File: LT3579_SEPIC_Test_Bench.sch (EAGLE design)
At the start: 160 parts

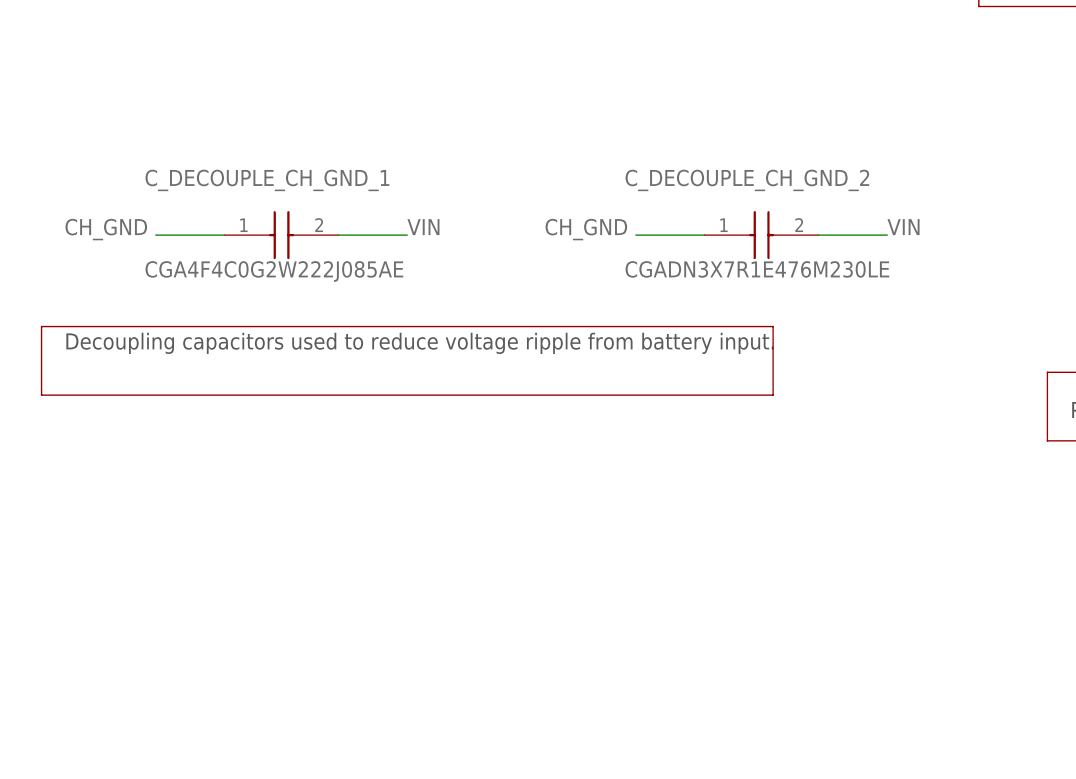
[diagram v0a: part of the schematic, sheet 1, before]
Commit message: Modified Text Sizes of Test Points, Addeed more GND Vias, Added Mounting Holes
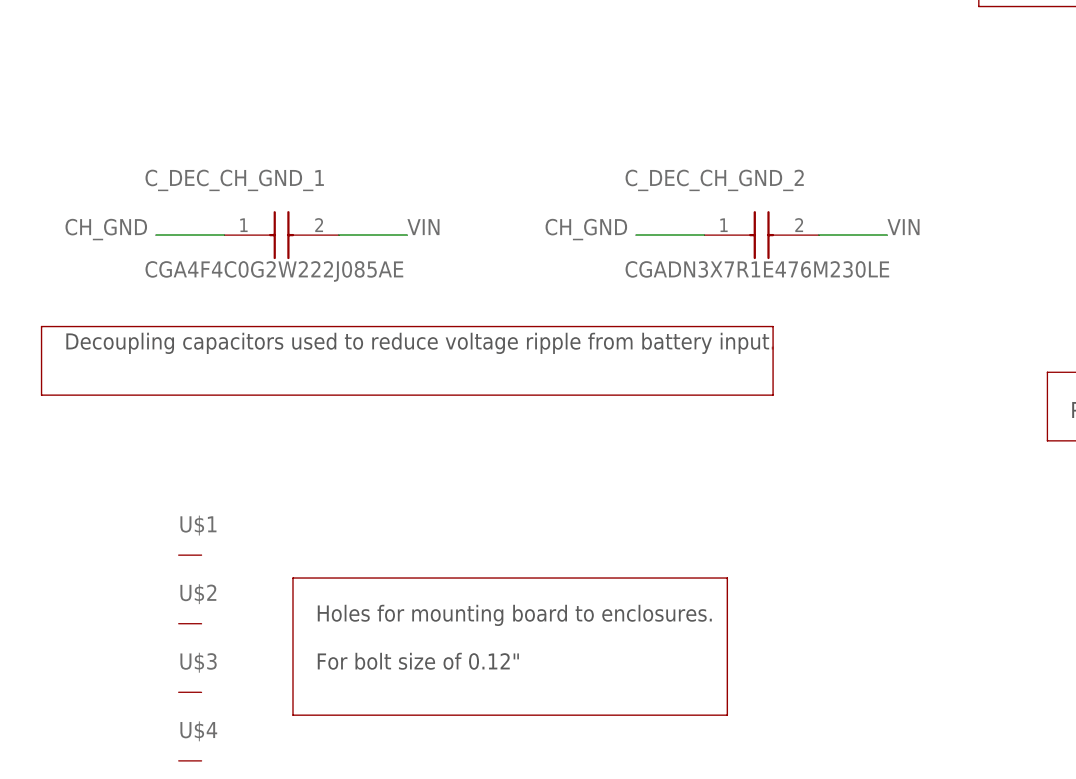
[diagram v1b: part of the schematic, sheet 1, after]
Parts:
- added U$1, U$2, U$3, U$4: THROUGH_HOLE_, THROUGH_HOLE:THROUGH_HOLE_
- renumbered C_DECOUPLE_CH_GND_1 to C_DEC_CH_GND_1, C_DECOUPLE_CH_GND_2 to C_DEC_CH_GND_2
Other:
- note added: "Holes for mounting board to enclosures. For bolt size of 0.12""
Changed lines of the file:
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@@
 <part name="R_FB_2" library="AC0805FR-0745K3L" deviceset="AC0805FR-0745K3L" device=""/>
 <part name="4P_INPUT_CONNECTOR1" library="SAMTEC-CLP-102-02-X-D" deviceset="SAMTEC-CLP-102-02-X-D" device="J"/>
-<part name="C_DECOUPLE_CH_GND_1" library="SamacSys_Parts" deviceset="CGA4F4C0G2W222J085AE" device=""/>
-<part name="C_DECOUPLE_CH_GND_2" library="SamacSys_Parts" deviceset="CGADN3X7R1E476M230LE" device=""/>
+<part name="C_DEC_CH_GND_1" library="SamacSys_Parts" deviceset="CGA4F4C0G2W222J085AE" device=""/>
+<part name="C_DEC_CH_GND_2" library="SamacSys_Parts" deviceset="CGADN3X7R1E476M230LE" device=""/>
 <part name="12P_OUTPUT_CONNECTOR1" library="SamacSys_Parts" deviceset="CLP-106-02-F-D" device=""/>
 <part name="GND2" library="supply1" library_urn="urn:adsk.eagle:library:371" deviceset="GND" device=""/>
@@
 <part name="NMOS_LDO_2" library="SamacSys_Parts" deviceset="RSR025N03HZGTL" device=""/>
 <part name="PMOS_REVERSE_V_PROTECTION" library="DMP3015LSSQ-13" deviceset="DMP3015LSSQ-13" device=""/>
+<part name="U$1" library="THROUGH_HOLE" deviceset="THROUGH_HOLE_" device=""/>
+<part name="U$2" library="THROUGH_HOLE" deviceset="THROUGH_HOLE_" device=""/>
+<part name="U$3" library="THROUGH_HOLE" deviceset="THROUGH_HOLE_" device=""/>
+<part name="U$4" library="THROUGH_HOLE" deviceset="THROUGH_HOLE_" device=""/>
 </parts>
 <sheets>
@@
 <wire x1="7.62" y1="40.64" x2="7.62" y2="48.26" width="0.1524" layer="94"/>
 <wire x1="7.62" y1="48.26" x2="-30.48" y2="48.26" width="0.1524" layer="94"/>
+<text x="-66.04" y="-66.04" size="1.778" layer="97">Holes for mounting board to enclosures.
+For bolt size of 0.12"</text>
+<wire x1="-68.58" y1="-55.88" x2="-68.58" y2="-71.12" width="0.1524" layer="94"/>
+<wire x1="-68.58" y1="-71.12" x2="-20.32" y2="-71.12" width="0.1524" layer="94"/>
+<wire x1="-20.32" y1="-71.12" x2="-20.32" y2="-55.88" width="0.1524" layer="94"/>
+<wire x1="-20.32" y1="-55.88" x2="-68.58" y2="-55.88" width="0.1524" layer="94"/>
 </plain>
 <instances>
@@
 <attribute name="VALUE" x="-68.58" y="22.86" size="2.286" layer="96"/>
 </instance>
-<instance part="C_DECOUPLE_CH_GND_1" gate="G$1" x="-76.2" y="-17.78" smashed="yes">
+<instance part="C_DEC_CH_GND_1" gate="G$1" x="-76.2" y="-17.78" smashed="yes">
 <attribute name="NAME" x="-85.09" y="-11.43" size="1.778" layer="95" align="center-left"/>
 <attribute name="VALUE" x="-85.09" y="-21.59" size="1.778" layer="96" align="center-left"/>
 </instance>
-<instance part="C_DECOUPLE_CH_GND_2" gate="G$1" x="-22.86" y="-17.78" smashed="yes">
+<instance part="C_DEC_CH_GND_2" gate="G$1" x="-22.86" y="-17.78" smashed="yes">
 <attribute name="NAME" x="-31.75" y="-11.43" size="1.778" layer="95" align="center-left"/>
 <attribute name="VALUE" x="-31.75" y="-21.59" size="1.778" layer="96" align="center-left"/>
@@
 <attribute name="VALUE" x="34.29" y="-8.89" size="1.778" layer="96"/>
 <attribute name="NAME" x="49.53" y="-24.13" size="1.778" layer="95"/>
+</instance>
+<instance part="U$1" gate="G$1" x="-81.28" y="-53.34" smashed="yes">
+<attribute name="NAME" x="-81.28" y="-50.8" size="1.778" layer="95"/>
+</instance>
+<instance part="U$2" gate="G$1" x="-81.28" y="-60.96" smashed="yes">
+<attribute name="NAME" x="-81.28" y="-58.42" size="1.778" layer="95"/>
+</instance>
+<instance part="U$3" gate="G$1" x="-81.28" y="-68.58" smashed="yes">
+<attribute name="NAME" x="-81.28" y="-66.04" size="1.778" layer="95"/>
+</instance>
+<instance part="U$4" gate="G$1" x="-81.28" y="-76.2" smashed="yes">
+<attribute name="NAME" x="-81.28" y="-73.66" size="1.778" layer="95"/>
 </instance>
 </instances>
@@
 <net name="VIN" class="4">
 <segment>
-<pinref part="C_DECOUPLE_CH_GND_1" gate="G$1" pin="2"/>
+<pinref part="C_DEC_CH_GND_1" gate="G$1" pin="2"/>
 <wire x1="-63.5" y1="-17.78" x2="-55.88" y2="-17.78" width="0.1524" layer="91"/>
 <label x="-55.88" y="-17.78" size="1.778" layer="95"/>
 </segment>
 <segment>
-<pinref part="C_DECOUPLE_CH_GND_2" gate="G$1" pin="2"/>
+<pinref part="C_DEC_CH_GND_2" gate="G$1" pin="2"/>
 <wire x1="-10.16" y1="-17.78" x2="-2.54" y2="-17.78" width="0.1524" layer="91"/>
 <label x="-2.54" y="-17.78" size="1.778" layer="95"/>
@@
 <net name="CH_GND" class="2">
 <segment>
-<pinref part="C_DECOUPLE_CH_GND_1" gate="G$1" pin="1"/>
+<pinref part="C_DEC_CH_GND_1" gate="G$1" pin="1"/>
 <wire x1="-76.2" y1="-17.78" x2="-83.82" y2="-17.78" width="0.1524" layer="91"/>
 <label x="-93.98" y="-17.78" size="1.778" layer="95"/>
 </segment>
 <segment>
-<pinref part="C_DECOUPLE_CH_GND_2" gate="G$1" pin="1"/>
+<pinref part="C_DEC_CH_GND_2" gate="G$1" pin="1"/>
 <wire x1="-22.86" y1="-17.78" x2="-30.48" y2="-17.78" width="0.1524" layer="91"/>
 <label x="-40.64" y="-17.78" size="1.778" layer="95"/>

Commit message: changed GND planes. Ready for review
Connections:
- removed net GND: 12P_OUTPUT_CONNECTOR1.10, 12P_OUTPUT_CONNECTOR1.12, 12P_OUTPUT_CONNECTOR1.8, C_68N_FILTER_.2, C_68N_FILTER_1.2, C_68N_FILTER_2.2, C_C_.2, C_C_1.2, C_C_2.2, C_F_.2, C_F_1.2, C_F_2.2, C_IN_1_.2, C_IN_1_1.2, C_IN_1_2.2, C_IN_2_.2, C_IN_2_1.2, C_IN_2_2.2, C_LDO_IN_.2, C_LDO_OUT_.2, C_LS_.2, C_LS_1.2, C_LS_2.2, C_OUT_1_.2, C_OUT_1_1.2, C_OUT_1_2.2, C_OUT_2_.2, C_OUT_2_1.2, C_OUT_2_2.2, C_OUT_3_.2, C_OUT_3_1.2, C_OUT_3_2.2, C_SS_.2, C_SS_1.2, C_SS_2.2, L1L2_.4, L1L2_1.4, L1L2_2.4, LDO_.GND, LED_.K, LED_1.K, LED_2.K, LT3579_IC_.EPAD, LT3579_IC_.SYNC, LT3579_IC_1.EPAD, LT3579_IC_1.SYNC, LT3579_IC_2.EPAD, LT3579_IC_2.SYNC, NMOS_LDO_.S, NMOS_LDO_1.S, NMOS_LDO_2.S, R_5K_FILTER_\.2, R_5K_FILTER_\1.2, R_5K_FILTER_\2.2, R_SHUNT_GND_.2, R_SHUNT_GND_1.2, R_SHUNT_GND_2.2, R_T_.2, R_T_1.2, R_T_2.2, R_UVLO2_.1, R_UVLO2_1.1, R_UVLO2_2.1, TP_GND1_.1, TP_GND1_1.1, TP_GND1_2.1, TP_GND2_.1, TP_GND2_1.1, TP_GND2_2.1, TP_GND3_.1, TP_GND3_1.1, TP_GND3_2.1, TP_GND4_.1, TP_GND4_1.1, TP_GND4_2.1, TP_GND_.1, TP_GND_1.1, TP_GND_2.1
- new net GND_: 12P_OUTPUT_CONNECTOR1.12, C_68N_FILTER_.2, C_C_.2, C_F_.2, C_IN_1_.2, C_IN_2_.2, C_LDO_IN_.2, C_LDO_OUT_.2, C_LS_.2, C_OUT_1_.2, C_OUT_2_.2, C_OUT_3_.2, C_SS_.2, L1L2_.4, LDO_.GND, LED_.K, LT3579_IC_.EPAD, LT3579_IC_.SYNC, NMOS_LDO_.S, R_5K_FILTER_\.2, R_SHUNT_GND_.2, R_T_.2, R_UVLO2_.1, TP_GND1_.1, TP_GND2_.1, TP_GND3_.1, TP_GND4_.1, TP_GND_.1
- new net GND_1: 12P_OUTPUT_CONNECTOR1.10, C_68N_FILTER_1.2, C_C_1.2, C_F_1.2, C_IN_1_1.2, C_IN_2_1.2, C_LS_1.2, C_OUT_1_1.2, C_OUT_2_1.2, C_OUT_3_1.2, C_SS_1.2, L1L2_1.4, LED_1.K, LT3579_IC_1.EPAD, LT3579_IC_1.SYNC, NMOS_LDO_1.S, R_5K_FILTER_\1.2, R_SHUNT_GND_1.2, R_T_1.2, R_UVLO2_1.1, TP_GND1_1.1, TP_GND2_1.1, TP_GND3_1.1, TP_GND4_1.1, TP_GND_1.1
- new net GND_2: 12P_OUTPUT_CONNECTOR1.8, C_68N_FILTER_2.2, C_C_2.2, C_F_2.2, C_IN_1_2.2, C_IN_2_2.2, C_LS_2.2, C_OUT_1_2.2, C_OUT_2_2.2, C_OUT_3_2.2, C_SS_2.2, L1L2_2.4, LED_2.K, LT3579_IC_2.EPAD, LT3579_IC_2.SYNC, NMOS_LDO_2.S, R_5K_FILTER_\2.2, R_SHUNT_GND_2.2, R_T_2.2, R_UVLO2_2.1, TP_GND1_2.1, TP_GND2_2.1, TP_GND3_2.1, TP_GND4_2.1, TP_GND_2.1
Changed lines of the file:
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@@
 <part name="C_DEC_CH_GND_2" library="SamacSys_Parts" deviceset="CGADN3X7R1E476M230LE" device=""/>
 <part name="12P_OUTPUT_CONNECTOR1" library="SamacSys_Parts" deviceset="CLP-106-02-F-D" device=""/>
-<part name="GND2" library="supply1" library_urn="urn:adsk.eagle:library:371" deviceset="GND" device=""/>
 <part name="R_10K_FILTER_" library="AC0805DR-0710KL" deviceset="AC0805DR-0710KL" device=""/>
 <part name="R_5K_FILTER_\" library="SamacSys_Parts" deviceset="RT1206BRD075KL" device=""/>
@@
 <attribute name="VALUE" x="29.21" y="38.1" size="1.778" layer="96" align="center-left"/>
 </instance>
-<instance part="GND2" gate="1" x="63.5" y="27.94" smashed="yes">
-<attribute name="VALUE" x="66.04" y="30.48" size="1.778" layer="96"/>
-</instance>
 <instance part="PMOS_REVERSE_V_PROTECTION" gate="G$1" x="45.72" y="-17.78" smashed="yes" rot="R90">
 <attribute name="VALUE" x="34.29" y="-8.89" size="1.778" layer="96"/>
@@
 </busses>
 <nets>
-<net name="GND" class="1">
-<segment>
-<pinref part="12P_OUTPUT_CONNECTOR1" gate="G$1" pin="8"/>
-<wire x1="50.8" y1="27.94" x2="55.88" y2="27.94" width="0.1524" layer="91"/>
-<pinref part="12P_OUTPUT_CONNECTOR1" gate="G$1" pin="10"/>
-<wire x1="50.8" y1="30.48" x2="55.88" y2="30.48" width="0.1524" layer="91"/>
-<wire x1="55.88" y1="27.94" x2="55.88" y2="30.48" width="0.1524" layer="91"/>
-<pinref part="12P_OUTPUT_CONNECTOR1" gate="G$1" pin="12"/>
-<wire x1="50.8" y1="33.02" x2="55.88" y2="33.02" width="0.1524" layer="91"/>
-<wire x1="55.88" y1="33.02" x2="55.88" y2="30.48" width="0.1524" layer="91"/>
-<wire x1="55.88" y1="30.48" x2="63.5" y2="30.48" width="0.1524" layer="91"/>
-<pinref part="GND2" gate="1" pin="GND"/>
-<junction x="55.88" y="30.48"/>
-</segment>
-</net>
 <net name="VIN" class="4">
 <segment>
@@
 <wire x1="50.8" y1="-15.24" x2="58.42" y2="-15.24" width="0.1524" layer="91"/>
 <label x="58.42" y="-15.24" size="1.778" layer="95"/>
+</segment>
+</net>
+<net name="GND_" class="0">
+<segment>
+<pinref part="12P_OUTPUT_CONNECTOR1" gate="G$1" pin="12"/>
+<wire x1="50.8" y1="33.02" x2="55.88" y2="33.02" width="0.1524" layer="91"/>
+<label x="55.88" y="33.02" size="1.778" layer="95"/>
+</segment>
+</net>
+<net name="GND_1" class="0">
+<segment>
+<pinref part="12P_OUTPUT_CONNECTOR1" gate="G$1" pin="10"/>
+<wire x1="50.8" y1="30.48" x2="55.88" y2="30.48" width="0.1524" layer="91"/>
+<label x="55.88" y="30.48" size="1.778" layer="95"/>
+</segment>
+</net>
+<net name="GND_2" class="0">
+<segment>
+<pinref part="12P_OUTPUT_CONNECTOR1" gate="G$1" pin="8"/>
+<wire x1="50.8" y1="27.94" x2="55.88" y2="27.94" width="0.1524" layer="91"/>
+<label x="55.88" y="27.94" size="1.778" layer="95"/>
 </segment>
 </net>
@@
 </segment>
 </net>
-<net name="GND" class="1">
+<net name="GND_" class="0">
 <segment>
 <pinref part="R_SHUNT_GND_" gate="G$1" pin="2"/>
@@
 <wire x1="-119.38" y1="106.68" x2="-119.38" y2="86.36" width="0.1524" layer="91"/>
 <junction x="-119.38" y="86.36"/>
+<label x="-119.38" y="91.44" size="1.778" layer="95"/>
 </segment>
 <segment>
@@
 </segment>
 </net>
-<net name="GND" class="1">
+<net name="GND_1" class="0">
 <segment>
 <pinref part="R_SHUNT_GND_1" gate="G$1" pin="2"/>
@@
 <wire x1="-111.76" y1="109.22" x2="-111.76" y2="88.9" width="0.1524" layer="91"/>
 <junction x="-111.76" y="88.9"/>
+<label x="-111.76" y="93.98" size="1.778" layer="95"/>
 </segment>
 <segment>
@@
 </segment>
 </net>
-<net name="GND" class="1">
+<net name="GND_2" class="0">
 <segment>
 <pinref part="R_SHUNT_GND_2" gate="G$1" pin="2"/>
@@
 <wire x1="-119.38" y1="101.6" x2="-119.38" y2="81.28" width="0.1524" layer="91"/>
 <junction x="-119.38" y="81.28"/>
-</segment>
-<segment>
+<label x="-116.84" y="86.36" size="1.778" layer="95"/>
+</segment>
+<segment>

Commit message: Changed Trace Widths of Signals
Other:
- note added: "Holes for mounting board to enclosures. For bolt size of 1/16""
- note removed: "Holes for mounting board to enclosures. For bolt size of 0.12""
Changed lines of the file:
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@@
 <class number="2" name="PWR_Vin_Vout" width="0.816" drill="0">
 </class>
-<class number="3" name="Signal" width="0.0463" drill="0">
+<class number="3" name="Signal" width="0.381" drill="0">
 </class>
 <class number="4" name="PWR_Vin" width="0.0463" drill="0">
@@
 <wire x1="7.62" y1="48.26" x2="-30.48" y2="48.26" width="0.1524" layer="94"/>
 <text x="-66.04" y="-66.04" size="1.778" layer="97">Holes for mounting board to enclosures.
-For bolt size of 0.12"</text>
+For bolt size of 1/16"</text>
 <wire x1="-68.58" y1="-55.88" x2="-68.58" y2="-71.12" width="0.1524" layer="94"/>
 <wire x1="-68.58" y1="-71.12" x2="-20.32" y2="-71.12" width="0.1524" layer="94"/>

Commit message: modified GND planes
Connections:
- net CH_GND: now also C_LDO_IN_.2, C_LDO_OUT_.2, LDO_.GND
- net GND_: no longer C_LDO_IN_.2, C_LDO_OUT_.2, LDO_.GND
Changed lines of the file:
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@@
-</segment>
-<segment>
-<pinref part="LDO_" gate="G$1" pin="GND"/>
-<wire x1="-190.5" y1="-58.42" x2="-195.58" y2="-58.42" width="0.1524" layer="91"/>
-<label x="-200.66" y="-58.42" size="1.778" layer="95"/>
 </segment>
 <segment>
@@
 </segment>
 <segment>
-<pinref part="C_LDO_IN_" gate="G$1" pin="2"/>
-<pinref part="X_50" gate="G$1" pin="0"/>
-<wire x1="-167.64" y1="-86.36" x2="-160.02" y2="-86.36" width="0.1524" layer="91"/>
-</segment>
-<segment>
-<pinref part="C_LDO_OUT_" gate="G$1" pin="2"/>
-<pinref part="X_49" gate="G$1" pin="0"/>
-<wire x1="-167.64" y1="-38.1" x2="-160.02" y2="-38.1" width="0.1524" layer="91"/>
-</segment>
-<segment>
 <pinref part="C_LS_" gate="G$1" pin="2"/>
 <pinref part="X_53" gate="G$1" pin="0"/>
@@
 <junction x="-121.92" y="-96.52"/>
 </segment>
+<segment>
+<pinref part="C_LDO_IN_" gate="G$1" pin="2"/>
+<pinref part="X_50" gate="G$1" pin="0"/>
+<wire x1="-167.64" y1="-86.36" x2="-160.02" y2="-86.36" width="0.1524" layer="91"/>
+<label x="-162.56" y="-81.28" size="1.778" layer="95"/>
+</segment>
+<segment>
+<pinref part="LDO_" gate="G$1" pin="GND"/>
+<wire x1="-190.5" y1="-58.42" x2="-195.58" y2="-58.42" width="0.1524" layer="91"/>
+<label x="-208.28" y="-58.42" size="1.778" layer="95"/>
+</segment>
+<segment>
+<pinref part="C_LDO_OUT_" gate="G$1" pin="2"/>
+<pinref part="X_49" gate="G$1" pin="0"/>
+<wire x1="-167.64" y1="-38.1" x2="-160.02" y2="-38.1" width="0.1524" layer="91"/>
+<label x="-162.56" y="-35.56" size="1.778" layer="95"/>
+</segment>
 </net>

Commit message: Added more GND Vias, Changes text size, moved texts, clears DRC error
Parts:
- renumbered C_68N_FILTER_ to C_68N_F_, C_68N_FILTER_1 to C_68N_F_1, C_68N_FILTER_2 to C_68N_F_2, R_10K_FILTER_ to R_10K_F_, R_10K_FILTER_1 to R_10K_F_1, R_10K_FILTER_2 to R_10K_F_2, R_5K_FILTER_\ to R_5K_F_, R_5K_FILTER_\1 to R_5K_F_1, R_5K_FILTER_\2 to R_5K_F_2, TP_CLK_FILTER_ to TP_CLK_F_, TP_CLK_FILTER_1 to TP_CLK_F_1, TP_CLK_FILTER_2 to TP_CLK_F_2

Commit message: Used SRC to change the LBR reference of each componant
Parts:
- 12P_OUTPUT_CONNECTOR1: device SamacSys_Parts:CLP-106-02-F-D -> LT3579_SEPIC_Test_Bench:CLP-106-02-F-D
- 4P_INPUT_CONNECTOR1: device SAMTEC-CLP-102-02-X-D:SAMTEC-CLP-102-02-X-DJ -> LT3579_SEPIC_Test_Bench:SAMTEC-CLP-102-02-X-DJ
- C_1_, C_1_1, C_1_2, C_IN_1_, C_IN_1_1, C_IN_1_2, C_IN_2_, C_IN_2_1, C_IN_2_2, C_OUT_1_, C_OUT_1_1, C_OUT_1_2, C_OUT_2_, C_OUT_2_1, C_OUT_2_2, C_OUT_3_, C_OUT_3_1, C_OUT_3_2: device SamacSys_Parts:CGA4J1X7R1E475K125AE -> LT3579_SEPIC_Test_Bench:CGA4J1X7R1E475K125AE
- C_68N_F_, C_68N_F_1, C_68N_F_2: device SamacSys_Parts:CEU4J2X7R1H683K125AE -> LT3579_SEPIC_Test_Bench:CEU4J2X7R1H683K125AE
- C_C_, C_C_1, C_C_2, C_DEC_CH_GND_1: device SamacSys_Parts:CGA4F4C0G2W222J085AE -> LT3579_SEPIC_Test_Bench:CGA4F4C0G2W222J085AE
- C_DEC_CH_GND_2: device SamacSys_Parts:CGADN3X7R1E476M230LE -> LT3579_SEPIC_Test_Bench:CGADN3X7R1E476M230LE
- C_F_, C_F_1, C_F_2: device SamacSys_Parts:CGA2B2C0G1H470J050BA -> LT3579_SEPIC_Test_Bench:CGA2B2C0G1H470J050BA
- C_LDO_IN_: device SamacSys_Parts:CGA3E1X7R1V105K080AC -> LT3579_SEPIC_Test_Bench:CGA3E1X7R1V105K080AC
- C_LDO_OUT_: device SamacSys_Parts:JMK107BB7475KA-T -> LT3579_SEPIC_Test_Bench:JMK107BB7475KA-T
- C_LS_, C_LS_1, C_LS_2: device SamacSys_Parts:CGA2B2C0G1H102J050BE -> LT3579_SEPIC_Test_Bench:CGA2B2C0G1H102J050BE
- C_SS_, C_SS_1, C_SS_2: device SamacSys_Parts:CGA4J2X8R1E224K125AE -> LT3579_SEPIC_Test_Bench:CGA4J2X8R1E224K125AE
- D1_, D1_1, D1_2: device SamacSys_Parts:MBRS330T3G -> LT3579_SEPIC_Test_Bench:MBRS330T3G
- L1L2_, L1L2_1, L1L2_2: device MSD1278T-Series:MSD1278T-XXXXX__ -> LT3579_SEPIC_Test_Bench:MSD1278T-XXXXX__
- LDO_: device SamacSys_Parts:LDL1117S33R -> LT3579_SEPIC_Test_Bench:LDL1117S33R
- LED_, LED_1, LED_2: device SamacSys_Parts:APTD1608LCGCK -> LT3579_SEPIC_Test_Bench:APTD1608LCGCK
- LT3579_IC_, LT3579_IC_1, LT3579_IC_2: device SamacSys_Parts:LT3579EFE#PBF -> LT3579_SEPIC_Test_Bench:LT3579EFE#PBF
- NMOS_LDO_, NMOS_LDO_1, NMOS_LDO_2: device SamacSys_Parts:RSR025N03HZGTL -> LT3579_SEPIC_Test_Bench:RSR025N03HZGTL
- PMOS_, PMOS_1, PMOS_2: device SamacSys_Parts:RQ5E050ATTCL -> LT3579_SEPIC_Test_Bench:RQ5E050ATTCL
- PMOS_REVERSE_V_PROTECTION: device DMP3015LSSQ-13:DMP3015LSSQ-13 -> LT3579_SEPIC_Test_Bench:DMP3015LSSQ-13
- R_10K_F_, R_10K_F_1, R_10K_F_2: device AC0805DR-0710KL:AC0805DR-0710KL -> LT3579_SEPIC_Test_Bench:AC0805DR-0710KL
- R_20K_LED1_: device SamacSys_Parts:ERJ-2RKF2002X -> LT3579_SEPIC_Test_Bench:ERJ-2RKF2002X
- R_5.6K_LED2_: device SamacSys_Parts:ERA-2ARB562X -> LT3579_SEPIC_Test_Bench:ERA-2ARB562X
- R_5K_F_, R_5K_F_1, R_5K_F_2, R_UVLO2_, R_UVLO2_1, R_UVLO2_2: device SamacSys_Parts:RT1206BRD075KL -> LT3579_SEPIC_Test_Bench:RT1206BRD075KL
- R_C_, R_C_1, R_C_2: device SamacSys_Parts:AC0805JR-0712KL -> LT3579_SEPIC_Test_Bench:AC0805JR-0712KL
- R_FAULT_, R_FAULT_1, R_FAULT_2, R_LS_GATE_, R_LS_GATE_1, R_LS_GATE_2: device AT0805FRE07100KL:AT0805FRE07100KL -> LT3579_SEPIC_Test_Bench:AT0805FRE07100KL
- R_FB_: device AC0805FR-07150KL:AC0805FR-07150KL -> LT3579_SEPIC_Test_Bench:AC0805FR-07150KL
- R_FB_1: device AC0603FR-0764K9L:AC0603FR-0764K9L -> LT3579_SEPIC_Test_Bench:AC0603FR-0764K9L
- R_FB_2: device AC0805FR-0745K3L:AC0805FR-0745K3L -> LT3579_SEPIC_Test_Bench:AC0805FR-0745K3L
- R_GATE_, R_GATE_1, R_GATE_2: device SamacSys_Parts:AC0805FR-0710KL -> LT3579_SEPIC_Test_Bench:AC0805FR-0710KL
- R_LED_10K_1, R_LED_10K_2, R_LS_DRAIN_, R_LS_DRAIN_1, R_LS_DRAIN_2: device SamacSys_Parts:MCS0402MD1002DE000 -> LT3579_SEPIC_Test_Bench:MCS0402MD1002DE000
- R_SHUNT_GND_, R_SHUNT_GND_1, R_SHUNT_GND_2: device GMR100HTCFAR100:GMR100HTCFAR100 -> LT3579_SEPIC_Test_Bench:GMR100HTCFAR100
- R_T_, R_T_1, R_T_2: device SamacSys_Parts:AC0805FR-07124KL -> LT3579_SEPIC_Test_Bench:AC0805FR-07124KL
- R_UVLO1_, R_UVLO1_1, R_UVLO1_2: device AC0805FR-0730KL:AC0805FR-0730KL -> LT3579_SEPIC_Test_Bench:AC0805FR-0730KL
- TP_CF_, TP_CF_1, TP_CF_2, TP_CH_GND_, TP_CH_GND_1, TP_CH_GND_2, TP_CLK_, TP_CLK_1, TP_CLK_2, TP_CLK_F_, TP_CLK_F_1, TP_CLK_F_2, TP_D1_, TP_D1_1, TP_D1_2, TP_FAULT_, TP_FAULT_1, TP_FAULT_2, TP_FAULT_LS_, TP_FAULT_LS_1, TP_FAULT_LS_2, TP_FB_, TP_FB_1, TP_FB_2, TP_GATE_, TP_GATE_1, TP_GATE_2, TP_GND1_, TP_GND1_1, TP_GND1_2, TP_GND2_, TP_GND2_1, TP_GND2_2, TP_GND3_, TP_GND3_1, TP_GND3_2, TP_GND4_, TP_GND4_1, TP_GND4_2, TP_GND_, TP_GND_1, TP_GND_2, TP_IN_, TP_IN_1, TP_IN_2, TP_LDO_OUT_, TP_OUT_, TP_OUT_1, TP_OUT_2, TP_RT_, TP_RT_1, TP_RT_2, TP_SHDN_, TP_SHDN_1, TP_SHDN_2, TP_SS_, TP_SS_1, TP_SS_2, TP_SW_, TP_SW_1, TP_SW_2: device S1751-46R:S1751-46R -> LT3579_SEPIC_Test_Bench:S1751-46R
- U$1, U$2, U$3, U$4: device THROUGH_HOLE:THROUGH_HOLE_ -> LT3579_SEPIC_Test_Bench:THROUGH_HOLE_

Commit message: Modifed board. Connected GND planes Together.
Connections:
- removed net GND_: 12P_OUTPUT_CONNECTOR1.12, C_68N_F_.2, C_C_.2, C_F_.2, C_IN_1_.2, C_IN_2_.2, C_LS_.2, C_OUT_1_.2, C_OUT_2_.2, C_OUT_3_.2, C_SS_.2, L1L2_.4, LED_.K, LT3579_IC_.EPAD, LT3579_IC_.SYNC, NMOS_LDO_.S, R_5K_F_.2, R_SHUNT_GND_.2, R_T_.2, R_UVLO2_.1, TP_GND1_.1, TP_GND2_.1, TP_GND3_.1, TP_GND4_.1, TP_GND_.1
- removed net GND_1: 12P_OUTPUT_CONNECTOR1.10, C_68N_F_1.2, C_C_1.2, C_F_1.2, C_IN_1_1.2, C_IN_2_1.2, C_LS_1.2, C_OUT_1_1.2, C_OUT_2_1.2, C_OUT_3_1.2, C_SS_1.2, L1L2_1.4, LED_1.K, LT3579_IC_1.EPAD, LT3579_IC_1.SYNC, NMOS_LDO_1.S, R_5K_F_1.2, R_SHUNT_GND_1.2, R_T_1.2, R_UVLO2_1.1, TP_GND1_1.1, TP_GND2_1.1, TP_GND3_1.1, TP_GND4_1.1, TP_GND_1.1
- removed net GND_2: 12P_OUTPUT_CONNECTOR1.8, C_68N_F_2.2, C_C_2.2, C_F_2.2, C_IN_1_2.2, C_IN_2_2.2, C_LS_2.2, C_OUT_1_2.2, C_OUT_2_2.2, C_OUT_3_2.2, C_SS_2.2, L1L2_2.4, LED_2.K, LT3579_IC_2.EPAD, LT3579_IC_2.SYNC, NMOS_LDO_2.S, R_5K_F_2.2, R_SHUNT_GND_2.2, R_T_2.2, R_UVLO2_2.1, TP_GND1_2.1, TP_GND2_2.1, TP_GND3_2.1, TP_GND4_2.1, TP_GND_2.1
- new net GND: 12P_OUTPUT_CONNECTOR1.10, 12P_OUTPUT_CONNECTOR1.12, 12P_OUTPUT_CONNECTOR1.8, C_68N_F_.2, C_68N_F_1.2, C_68N_F_2.2, C_C_.2, C_C_1.2, C_C_2.2, C_F_.2, C_F_1.2, C_F_2.2, C_IN_1_.2, C_IN_1_1.2, C_IN_1_2.2, C_IN_2_.2, C_IN_2_1.2, C_IN_2_2.2, C_LS_.2, C_LS_1.2, C_LS_2.2, C_OUT_1_.2, C_OUT_1_1.2, C_OUT_1_2.2, C_OUT_2_.2, C_OUT_2_1.2, C_OUT_2_2.2, C_OUT_3_.2, C_OUT_3_1.2, C_OUT_3_2.2, C_SS_.2, C_SS_1.2, C_SS_2.2, L1L2_.4, L1L2_1.4, L1L2_2.4, LED_.K, LED_1.K, LED_2.K, LT3579_IC_.EPAD, LT3579_IC_.SYNC, LT3579_IC_1.EPAD, LT3579_IC_1.SYNC, LT3579_IC_2.EPAD, LT3579_IC_2.SYNC, NMOS_LDO_.S, NMOS_LDO_1.S, NMOS_LDO_2.S, R_5K_F_.2, R_5K_F_1.2, R_5K_F_2.2, R_SHUNT_GND_.2, R_SHUNT_GND_1.2, R_SHUNT_GND_2.2, R_T_.2, R_T_1.2, R_T_2.2, R_UVLO2_.1, R_UVLO2_1.1, R_UVLO2_2.1, TP_GND1_.1, TP_GND1_1.1, TP_GND1_2.1, TP_GND2_.1, TP_GND2_1.1, TP_GND2_2.1, TP_GND3_.1, TP_GND3_1.1, TP_GND3_2.1, TP_GND4_.1, TP_GND4_1.1, TP_GND4_2.1, TP_GND_.1, TP_GND_1.1, TP_GND_2.1
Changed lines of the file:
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@@
 <setting verticaltext="up"/>
 </settings>
-<grid distance="0.1" unitdist="inch" unit="inch" style="lines" multiple="1" display="yes" altdistance="0.01" altunitdist="inch" altunit="inch"/>
+<grid distance="0.1" unitdist="inch" unit="inch" style="lines" multiple="1" display="no" altdistance="0.01" altunitdist="inch" altunit="inch"/>
 <layers>
 <layer number="1" name="Top" color="4" fill="1" visible="no" active="no"/>
@@
 </segment>
 </net>
-<net name="GND_" class="0">
+<net name="GND" class="0">
 <segment>
 <pinref part="12P_OUTPUT_CONNECTOR1" gate="G$1" pin="12"/>
@@
 <label x="55.88" y="33.02" size="1.778" layer="95"/>
 </segment>
-</net>
-<net name="GND_1" class="0">
 <segment>
 <pinref part="12P_OUTPUT_CONNECTOR1" gate="G$1" pin="10"/>
@@
 <label x="55.88" y="30.48" size="1.778" layer="95"/>
 </segment>
-</net>
-<net name="GND_2" class="0">
 <segment>
 <pinref part="12P_OUTPUT_CONNECTOR1" gate="G$1" pin="8"/>
@@
 </segment>
 </net>
-<net name="GND_" class="0">
+<net name="GND" class="0">
 <segment>
 <pinref part="R_SHUNT_GND_" gate="G$1" pin="2"/>
@@
 </segment>
 </net>
-<net name="GND_1" class="0">
+<net name="GND" class="0">
 <segment>
 <pinref part="R_SHUNT_GND_1" gate="G$1" pin="2"/>
@@
 </segment>
 </net>
-<net name="GND_2" class="0">
+<net name="GND" class="0">
 <segment>
 <pinref part="R_SHUNT_GND_2" gate="G$1" pin="2"/>
